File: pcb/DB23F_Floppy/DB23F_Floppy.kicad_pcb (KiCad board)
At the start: 2 copper layers, 40 x 12 mm, 3 parts, among them J1 DB23F solder cups, J2 Pins to motherboard, J3 Manual shield straps

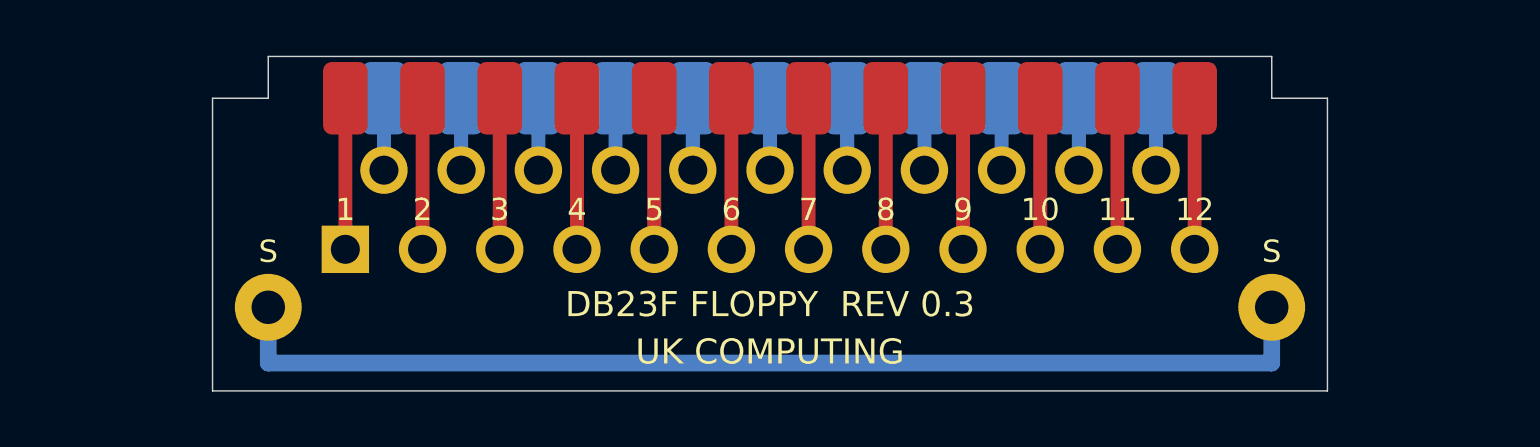
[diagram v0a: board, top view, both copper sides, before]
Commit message: Add bolted DB23 base and clip-on cap for revision 0.5
Shorten both adapter PCBs to Y13, add mounting ears at the original shell anchors, and separate the shell-wire pads from the nut-bearing lands. Preserve all 23 independent signal circuits.

Replace recessed top screw heads with upward M3 mounting screws, a solid printed base with integrated feet, and a keyed black cap. Add clip-fit coupons, updated loading jig, reference-driven corner reliefs and an insulated underside screw-head stack with deliberate shell-ground wiring.

Regenerate native KiCad projects, fit-prototype manufacturing files, printable STL/STEP, previews, five-page drawings, BOM, assembly guide and AI handover. Both native PCB DRC reports are clean; 648 electrical, 176 mechanical and 68 reference/alignment checks pass within their recorded scope. Physical fit, printed strength and Amiga operation remain untested.
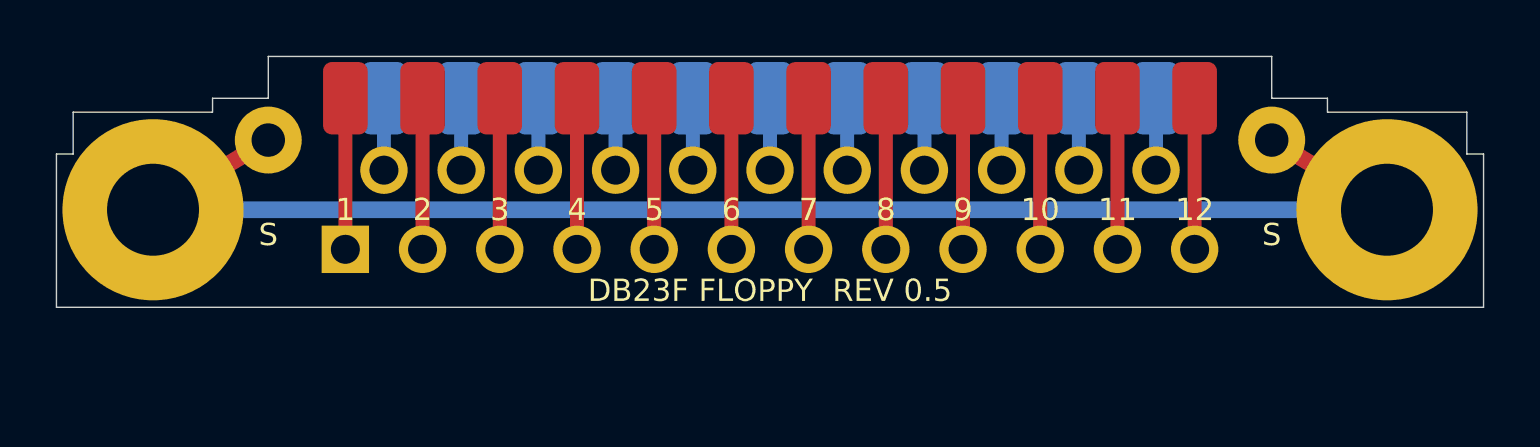
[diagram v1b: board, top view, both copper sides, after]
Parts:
- added J4: DB23 shell wire bond, DB23_Local:ShellBond_F, F.Cu at (150.0, 80.0)
- J3: value Manual shield straps -> M3 mounting / shield; footprint DB23_Local:ShieldStraps_F -> DB23_Local:MountingShield_F
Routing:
- net /SHIELD: track 40.0 -> 53.9 mm
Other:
- board size 40 x 12 mm -> 51.2 x 9 mm
- board text added: "DB23F FLOPPY REV 0.5"
- board text added: "UK COMPUTING 0.5"
- board text removed: "1:1 - 2.77 mm"
- board text removed: "DB23F FLOPPY REV 0.3"
- board text removed: "FIT PROTOTYPE"
- board text removed: "UK COMPUTING"

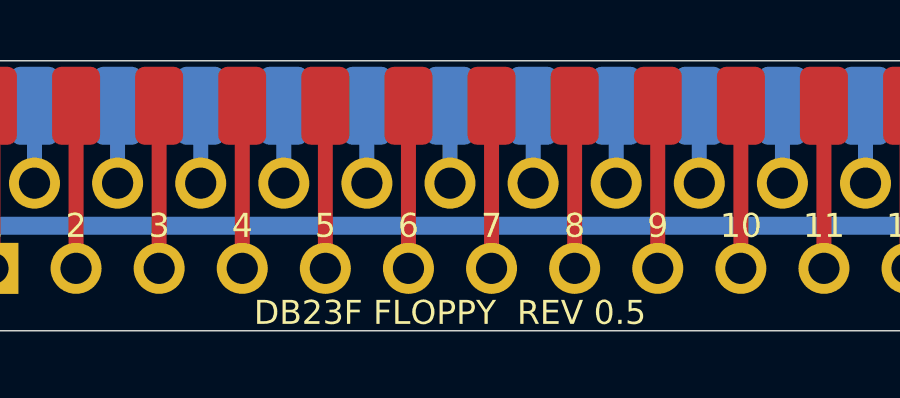
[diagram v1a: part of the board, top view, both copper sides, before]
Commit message: Refine DB23 end walls, PCB labels and project credits
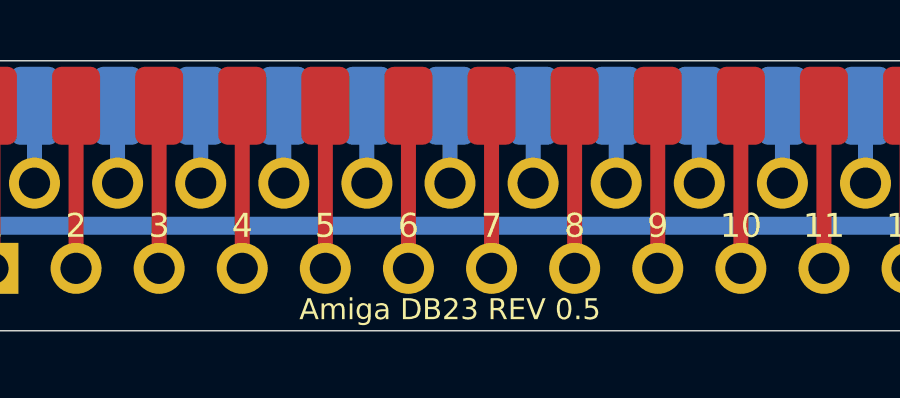
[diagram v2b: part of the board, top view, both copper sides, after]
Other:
- board text added: "Amiga DB23 REV 0.5"
- board text removed: "DB23F FLOPPY REV 0.5"
- board text removed: "UK COMPUTING 0.5"
